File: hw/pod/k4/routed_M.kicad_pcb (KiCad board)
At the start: 6 copper layers, 15.5 x 12 mm, 38 parts, among them J10 TestPoint_Pad_D1.0mm, J11 TestPoint_Pad_D1.0mm, J20 CONN-SMD_BM28B0.6-30DS-2-0.35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, J3 TestPoint_Pad_D1.0mm, J4 WirePad_1.0x2.0mm, J5 TestPoint_Pad_D1.0mm, J7 TestPoint_Pad_D1.0mm, J8 TestPoint_Pad_D1.0mm, J9 TestPoint_Pad_D1.0mm, SW1 SW-SMD_4P-L3.0-W2.6-P1.85-LS3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, U2 Knowles_LGA-5_3.5x2.65mm, U3 DSBGA-8_L1.6-W0.9-R2-C4-P0.40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, U4 X2SON-4_L1.0-W1.0-P0.65-TL-EP, U6 SOT-553-5_L1.6-W1.2-P0.50-LS1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

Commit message: K4 routed boards: apply Value fields from values_P/M.json (no copper change; DRC 0/0 both)
Co-Authored-By: Claude Opus 5.5 <noreply@anthropic.com>
Claude-Session: https://claude.ai/code/session_01Wg997D6KFs8bxoAH56jZZJ
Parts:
- C13, C19: value C_0201_0603Metric -> 100n
- C15: value C_0402_1005Metric -> 4u7 25V
- C16: value C_0201_0603Metric -> 2u2 10V
- C17: value C_0201_0603Metric -> 1u 16V
- C18: value C_0402_1005Metric -> 1u
- C21: value C_0402_1005Metric -> 10u
- D4: value D_SOD-882 -> PMEG3005EL
- D5: value X1SON-2_L1.0-W0.6-P0.65-BI-1 -> TPD1E10B06DPYR
- J10: value TestPoint_Pad_D1.0mm -> D+
- J11: value TestPoint_Pad_D1.0mm -> D-
- J20: value CONN-SMD_BM28B0.6-30DS-2-0.35V-51 -> BM28B0.6-30DS/2-0.35V(51)
- J3: value TestPoint_Pad_D1.0mm -> VBUS
- J4: value WirePad_1.0x2.0mm -> GND
- J5: value TestPoint_Pad_D1.0mm -> BAT+
- J7: value TestPoint_Pad_D1.0mm -> LED+
- J8: value TestPoint_Pad_D1.0mm -> LED-
- J9: value TestPoint_Pad_D1.0mm -> NTC
- R10, R14: value R_0201_0603Metric -> 2k2
- R12, R13: value R_0201_0603Metric -> 100k
- R15, R16: value R_0201_0603Metric -> 10k
- R20: value R_0402_1005Metric -> 0
- R30: value R_0402_1005Metric -> 33
- R8, R9: value R_0201_0603Metric -> 1M
- RT1: value R_0201_0603Metric -> 10k B3435
- SW1: value SW-SMD_4P-L3.0-W2.6-P1.85-LS3.4 -> KMT022NGJLHS
- TP10: value TestDot_D0.5mm -> MIC_DATA
- TP4: value TestPoint_Pad_D0.7mm -> 3V0
- TP5: value TestPoint_Pad_D0.7mm -> GND
- TP6: value TestPoint_Pad_D0.7mm -> VSYS
- U2: value Knowles_LGA-5_3.5x2.65mm -> SPH0641LU4H-1
- U3: value DSBGA-8_L1.6-W0.9-R2-C4-P0.40-BL -> BQ25180YBGR
- U4: value X2SON-4_L1.0-W1.0-P0.65-TL-EP -> TPS7A2030PDQNR
- U6: value SOT-553-5_L1.6-W1.2-P0.50-LS1.6-TL-1 -> TPD2E2U06DRLR
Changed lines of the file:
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@@
 			)
 		)
-		(property "Value" "X2SON-4_L1.0-W1.0-P0.65-TL-EP"
+		(property "Value" "TPS7A2030PDQNR"
 			(at 0 4.325 0)
 			(layer "F.Fab")
@@
 			)
 		)
-		(property "Value" "C_0201_0603Metric"
+		(property "Value" "2u2 10V"
 			(at 0 1.05 90)
 			(layer "F.Fab")
@@
 			)
 		)
-		(property "Value" "R_0201_0603Metric"
+		(property "Value" "100k"
 			(at 0 1.05 0)
 			(layer "F.Fab")
@@
 			)
 		)
-		(property "Value" "R_0201_0603Metric"
+		(property "Value" "1M"
 			(at 0 1.05 0)
 			(layer "F.Fab")
@@
 			)
 		)
-		(property "Value" "D_SOD-882"
+		(property "Value" "PMEG3005EL"
 			(at 0 1.35 90)
 			(layer "F.Fab")
@@
 			)
 		)
-		(property "Value" "C_0201_0603Metric"
+		(property "Value" "1u 16V"
 			(at 0 1.05 90)
 			(layer "F.Fab")
@@
 			)
 		)
-		(property "Value" "Knowles_LGA-5_3.5x2.65mm"
+		(property "Value" "SPH0641LU4H-1"
 			(at 0 3 0)
 			(layer "F.Fab")
@@
 			)
 		)
-		(property "Value" "DSBGA-8_L1.6-W0.9-R2-C4-P0.40-BL"
+		(property "Value" "BQ25180YBGR"
 			(at 0 4.2 90)
 			(layer "F.Fab")
@@
 			)
 		)
-		(property "Value" "R_0201_0603Metric"
+		(property "Value" "1M"
 			(at 0 1.05 0)
 			(layer "F.Fab")
@@
 			)
 		)
-		(property "Value" "CONN-SMD_BM28B0.6-30DS-2-0.35V-51"
+		(property "Value" "BM28B0.6-30DS/2-0.35V(51)"
 			(at 0 4.795 0)
 			(layer "F.Fab")
@@
 			)
 		)
-		(property "Value" "R_0201_0603Metric"
+		(property "Value" "2k2"
 			(at 0 1.05 0)
 			(layer "F.Fab")
@@
 			)
 		)
-		(property "Value" "C_0201_0603Metric"
+		(property "Value" "100n"
 			(at 0 1.05 90)
 			(layer "F.Fab")
@@
 			)
 		)
-		(property "Value" "R_0201_0603Metric"
+		(property "Value" "100k"
 			(at 0 1.05 0)
 			(layer "F.Fab")
@@
 			)
 		)
-		(property "Value" "X1SON-2_L1.0-W0.6-P0.65-BI-1"
+		(property "Value" "TPD1E10B06DPYR"
 			(at 0 4 0)
 			(layer "F.Fab")
@@
 			)
 		)
-		(property "Value" "R_0402_1005Metric"
+		(property "Value" "0"
 			(at 0 -1.17 0)
 			(layer "B.Fab")
@@
 			)
 		)
-		(property "Value" "SOT-553-5_L1.6-W1.2-P0.50-LS1.6-TL-1"
+		(property "Value" "TPD2E2U06DRLR"
 			(at 0 -4.5 90)
 			(layer "B.Fab")
@@
 			)
 		)
-		(property "Value" "TestPoint_Pad_D1.0mm"
+		(property "Value" "LED+"
 			(at 0 -1.55 0)
 			(layer "B.Fab")
@@
 			)
 		)
-		(property "Value" "R_0201_0603Metric"
+		(property "Value" "10k B3435"
 			(at 0 -1.05 90)
 			(layer "B.Fab")
@@
 			)
 		)
-		(property "Value" "TestDot_D0.5mm"
+		(property "Value" "MIC_DATA"
 			(at 0 -0.9 0)
 			(layer "B.Fab")
@@
 			)
 		)
-		(property "Value" "TestPoint_Pad_D1.0mm"
+		(property "Value" "NTC"
 			(at 0 -1.55 0)
 			(layer "B.Fab")
@@
 			)
 		)
-		(property "Value" "TestPoint_Pad_D1.0mm"
+		(property "Value" "D+"
 			(at 0 -1.55 0)
 			(layer "B.Fab")
@@
 			)
 		)
-		(property "Value" "R_0201_0603Metric"
+		(property "Value" "2k2"
 			(at 0 -1.05 0)
 			(layer "B.Fab")
@@
 			)
 		)
-		(property "Value" "R_0201_0603Metric"
+		(property "Value" "10k"
 			(at 0 -1.05 0)
 			(layer "B.Fab")
@@
 			)
 		)
-		(property "Value" "TestPoint_Pad_D1.0mm"
+		(property "Value" "VBUS"
 			(at 0 -1.55 0)
 			(layer "B.Fab")
@@
 			)
 		)
-		(property "Value" "C_0201_0603Metric"
+		(property "Value" "100n"
 			(at 0 -1.05 0)
 			(layer "B.Fab")
@@
 			)
 		)
-		(property "Value" "TestPoint_Pad_D0.7mm"
+		(property "Value" "GND"
 			(at 0 -0.9 0)
 			(layer "B.Fab")
@@
 			)
 		)
-		(property "Value" "TestPoint_Pad_D0.7mm"
+		(property "Value" "3V0"
 			(at 0 -0.9 0)
 			(layer "B.Fab")
@@
 			)
 		)
-		(property "Value" "C_0402_1005Metric"
+		(property "Value" "4u7 25V"
 			(at 0 -1.16 90)
 			(layer "B.Fab")
@@
 			)
 		)
-		(property "Value" "TestPoint_Pad_D1.0mm"
+		(property "Value" "D-"
 			(at 0 -1.55 0)
 			(layer "B.Fab")
@@
 			)
 		)
-		(property "Value" "C_0402_1005Metric"
+		(property "Value" "10u"
 			(at 0 -1.16 90)
 			(layer "B.Fab")
@@
 			)
 		)
-		(property "Value" "WirePad_1.0x2.0mm"
+		(property "Value" "GND"
 			(at 0 -0.9 0)
 			(layer "B.Fab")
@@
 			)
 		)
-		(property "Value" "C_0402_1005Metric"
+		(property "Value" "1u"
 			(at 0 -1.16 90)
 			(layer "B.Fab")
@@
 			)
 		)
-		(property "Value" "R_0201_0603Metric"
+		(property "Value" "10k"
 			(at 0 -1.05 0)
 			(layer "B.Fab")
@@
 			)
 		)
-		(property "Value" "TestPoint_Pad_D1.0mm"
+		(property "Value" "LED-"
 			(at 0 -1.55 0)
 			(layer "B.Fab")
@@
 			)
 		)
-		(property "Value" "SW-SMD_4P-L3.0-W2.6-P1.85-LS3.4"
+		(property "Value" "KMT022NGJLHS"
 			(at 0 -4.925 0)
 			(layer "B.Fab")
@@
 			)
 		)
-		(property "Value" "R_0402_1005Metric"
+		(property "Value" "33"
 			(at 0 -1.17 90)
 			(layer "B.Fab")
@@
 			)
 		)
-		(property "Value" "TestPoint_Pad_D0.7mm"
+		(property "Value" "VSYS"
 			(at 0 -0.9 0)
 			(layer "B.Fab")
@@
 			)
 		)
-		(property "Value" "TestPoint_Pad_D1.0mm"
+		(property "Value" "BAT+"
 			(at 0 -1.55 0)
 			(layer "B.Fab")

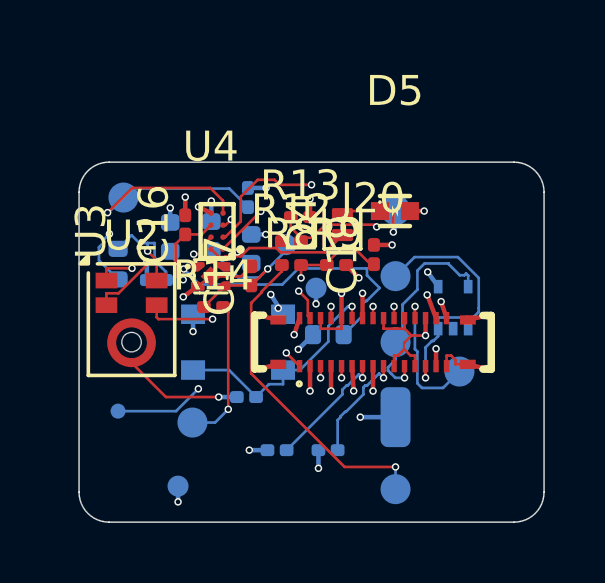
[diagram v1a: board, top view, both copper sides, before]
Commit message: K4 boards: clear all DRC warnings (refdes hidden, flagged silk removed, redundant GB_P via/stubs); release rebuilt on new hashes
Co-Authored-By: Claude Opus 5.5 <noreply@anthropic.com>
Claude-Session: https://claude.ai/code/session_01Wg997D6KFs8bxoAH56jZZJ
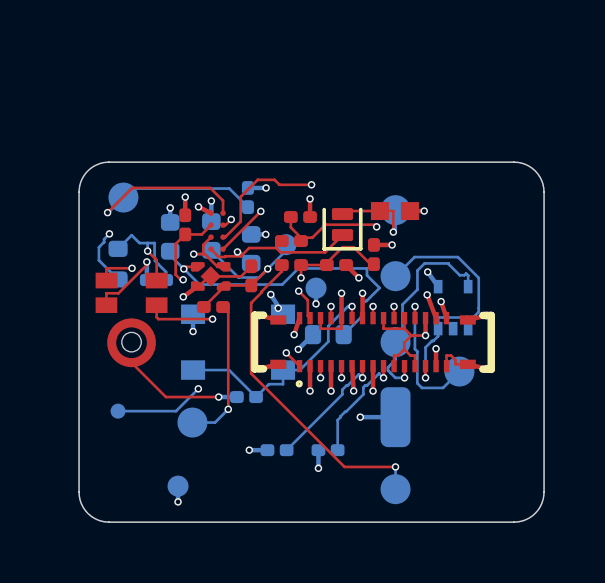
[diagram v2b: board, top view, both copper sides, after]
